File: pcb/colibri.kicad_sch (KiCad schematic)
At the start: 93 parts

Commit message: starting to build the right side
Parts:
- added pro-micro2: ProMicro, kbd:ProMicro_v4, symbol kbd:ProMicro
- added rd-1, rd-10, rd-11, rd-12, rd-13, rd-14, rd-15, rd-16, rd-17, rd-18, rd-19, rd-2, rd-20, rd-21, rd-22, rd-23, rd-24, rd-25, rd-26, rd-27, rd-3, rd-4, rd-5, rd-6, rd-7, rd-8, rd-9: 1N4148W, kbd:D3_SMD_v2, symbol Diode:1N4148W
- added rjack-1: MJ-4PP-9, kbd:MJ-4PP-9_1side, symbol kbd:MJ-4PP-9
- added rled-1, rled-10, rled-11, rled-12, rled-13, rled-14, rled-15, rled-16, rled-17, rled-18, rled-19, rled-2, rled-20, rled-21, rled-22, rled-23, rled-24, rled-25, rled-26, rled-27, rled-3, rled-4, rled-5, rled-6, rled-7, rled-8, rled-9: YS-SK6812MINI-E, kbd:YS-SK6812MINI-E, symbol kbd:YS-SK6812MINI-E
- added rreset-1: SW_PUSH, kbd:ResetSW_4P, symbol kbd:SW_PUSH
- added rsw-1: SW_PUSH, kbd:CherryMX_Hotswap_2u, symbol kbd:SW_PUSH
- added rsw-10, rsw-11, rsw-12, rsw-14, rsw-15, rsw-16, rsw-17, rsw-18, rsw-2, rsw-20, rsw-21, rsw-22, rsw-23, rsw-24, rsw-3, rsw-4, rsw-5, rsw-6, rsw-8, rsw-9: SW_PUSH, kbd:CherryMX_Hotswap, symbol kbd:SW_PUSH
- added rsw-13: SW_PUSH, kbd:CherryMX_Hotswap_2.25u, symbol kbd:SW_PUSH
- added rsw-19: SW_PUSH, kbd:CherryMX_Hotswap_2.75u, symbol kbd:SW_PUSH
- added rsw-25, rsw-26, rsw-27: SW_PUSH, kbd:CherryMX_Hotswap_1.25u, symbol kbd:SW_PUSH
- added rsw-7: SW_PUSH, kbd:CherryMX_Hotswap_1.5u, symbol kbd:SW_PUSH
- added ru-1, ru-2, ru-3, ru-4, ru-5, ru-6: WS2812B, LED_SMD:LED_WS2812B_PLCC4_5.0x5.0mm_P3.2mm, symbol LED:WS2812B
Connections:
- new net: rd-6.2 (A), rsw-6.2
- new net: rled-24.2 (DOUT), rled-27.4 (DIN)
- new net: rled-20.2 (DOUT), rled-21.4 (DIN)
- new net: rled-14.2 (DOUT), rled-20.4 (DIN)
- new net: rd-18.2 (A), rsw-18.2
- new net: rd-9.2 (A), rsw-9.2
- new net: rled-1.2 (DOUT), rled-2.4 (DIN)
- new net: rled-1.4 (DIN), rled-7.2 (DOUT)
- new net: rd-1.2 (A), rsw-1.2
- new net: rd-7.2 (A), rsw-7.2
- new net: rled-2.2 (DOUT), rled-8.4 (DIN)
- new net: rd-19.2 (A), rsw-19.2
- new net: rd-25.2 (A), rsw-25.2
- new net: rd-17.2 (A), rsw-17.2
- new net: rd-15.2 (A), rsw-15.2
- new net: rled-19.4 (DIN), ru-4.2 (DOUT)
- new net: ru-4.4 (DIN), ru-5.2 (DOUT)
- new net: rled-18.2 (DOUT), rled-24.4 (DIN)
- new net: rd-20.2 (A), rsw-20.2
- new net: rled-5.2 (DOUT), rled-6.4 (DIN)
- new net: rled-11.2 (DOUT), rled-5.4 (DIN)
- new net: rd-3.2 (A), rsw-3.2
- new net: rd-8.2 (A), rsw-8.2
- new net: ru-1.2 (DOUT), ru-2.4 (DIN)
- new net: rled-3.4 (DIN), rled-9.2 (DOUT)
- new net: rled-15.2 (DOUT), rled-9.4 (DIN)
- new net: rd-11.2 (A), rsw-11.2
- new net: rd-27.2 (A), rsw-27.2
- new net: rd-12.2 (A), rsw-12.2
- new net: rled-11.4 (DIN), rled-17.2 (DOUT)
- new net: rd-22.2 (A), rsw-22.2
- new net: rd-26.2 (A), rsw-26.2
- new net: ru-5.4 (DIN), ru-6.2 (DOUT)
- new net: rled-13.2 (DOUT), rled-7.4 (DIN)
- new net: rled-13.4 (DIN), rled-19.2 (DOUT)
- new net: rd-16.2 (A), rsw-16.2
- new net: rd-4.2 (A), rsw-4.2
- new net: rled-25.2 (DOUT), rled-26.4 (DIN)
- new net: rled-22.2 (DOUT), rled-25.4 (DIN)
- new net: ru-3.2 (DOUT), ru-6.4 (DIN)
- new net: ru-2.2 (DOUT), ru-3.4 (DIN)
- new net: rled-16.2 (DOUT), rled-22.4 (DIN)
- new net: rled-10.2 (DOUT), rled-16.4 (DIN)
- new net: rd-2.2 (A), rsw-2.2
- new net: rd-21.2 (A), rsw-21.2
- new net: rled-17.4 (DIN), rled-23.2 (DOUT)
- new net: rled-23.4 (DIN), rled-26.2 (DOUT)
- new net: rd-13.2 (A), rsw-13.2
- new net: rled-10.4 (DIN), rled-4.2 (DOUT)
- new net: rled-3.2 (DOUT), rled-4.4 (DIN)
- new net: rled-14.4 (DIN), rled-8.2 (DOUT)
- new net: rled-12.2 (DOUT), rled-18.4 (DIN)
- new net: rd-24.2 (A), rsw-24.2
- new net: rled-15.4 (DIN), rled-21.2 (DOUT)
- new net: rd-23.2 (A), rsw-23.2
- new net: rled-12.4 (DIN), rled-6.2 (DOUT)
- new net: rd-14.2 (A), rsw-14.2
- new net: rd-5.2 (A), rsw-5.2
- new net: rd-10.2 (A), rsw-10.2
- new net rGND: pro-micro2.23 (GND), pro-micro2.3 (GND), pro-micro2.4 (GND), rjack-1.C, rled-1.3 (VSS), rled-10.3 (VSS), rled-11.3 (VSS), rled-12.3 (VSS), rled-13.3 (VSS), rled-14.3 (VSS), rled-15.3 (VSS), rled-16.3 (VSS), rled-17.3 (VSS), rled-18.3 (VSS), rled-19.3 (VSS), rled-2.3 (VSS), rled-20.3 (VSS), rled-21.3 (VSS), rled-22.3 (VSS), rled-23.3 (VSS), rled-24.3 (VSS), rled-25.3 (VSS), rled-26.3 (VSS), rled-27.3 (VSS), rled-3.3 (VSS), rled-4.3 (VSS), rled-5.3 (VSS), rled-6.3 (VSS), rled-7.3 (VSS), rled-8.3 (VSS), rled-9.3 (VSS), rreset-1.2, ru-1.3 (VSS), ru-2.3 (VSS), ru-3.3 (VSS), ru-4.3 (VSS), ru-5.3 (VSS), ru-6.3 (VSS)
- new net rVCC: pro-micro2.21 (VCC), rjack-1.D, rled-1.1 (VDD), rled-10.1 (VDD), rled-11.1 (VDD), rled-12.1 (VDD), rled-13.1 (VDD), rled-14.1 (VDD), rled-15.1 (VDD), rled-16.1 (VDD), rled-17.1 (VDD), rled-18.1 (VDD), rled-19.1 (VDD), rled-2.1 (VDD), rled-20.1 (VDD), rled-21.1 (VDD), rled-22.1 (VDD), rled-23.1 (VDD), rled-24.1 (VDD), rled-25.1 (VDD), rled-26.1 (VDD), rled-27.1 (VDD), rled-3.1 (VDD), rled-4.1 (VDD), rled-5.1 (VDD), rled-6.1 (VDD), rled-7.1 (VDD), rled-8.1 (VDD), rled-9.1 (VDD), ru-1.1 (VDD), ru-2.1 (VDD), ru-3.1 (VDD), ru-4.1 (VDD), ru-5.1 (VDD), ru-6.1 (VDD)
- new net rcol0: pro-micro2.15 (B3/14), rsw-1.1, rsw-13.1, rsw-19.1, rsw-7.1
- new net rcol1: pro-micro2.16 (B1/15), rsw-14.1, rsw-2.1, rsw-20.1, rsw-8.1
- new net rcol2: pro-micro2.17 (F7/A0), rsw-15.1, rsw-21.1, rsw-3.1, rsw-9.1
- new net rcol3: pro-micro2.18 (F6/A1), rsw-10.1, rsw-16.1, rsw-22.1, rsw-25.1, rsw-4.1
- new net rcol4: pro-micro2.13 (B6/10), rsw-11.1, rsw-17.1, rsw-23.1, rsw-26.1, rsw-5.1
- new net rcol5: pro-micro2.14 (B2/16), rsw-12.1, rsw-18.1, rsw-24.1, rsw-27.1, rsw-6.1
- new net rdata: pro-micro2.2 (RX1/D2), rjack-1.B
- new net rled: pro-micro2.1 (TX0/D3), ru-1.4 (DIN)
- new net rreset: pro-micro2.22 (RST), rreset-1.1
- new net rrow0: pro-micro2.8 (5/C6), rd-1.1 (K), rd-2.1 (K), rd-3.1 (K), rd-4.1 (K), rd-5.1 (K), rd-6.1 (K)
- new net rrow1: pro-micro2.9 (6/D7), rd-10.1 (K), rd-11.1 (K), rd-12.1 (K), rd-7.1 (K), rd-8.1 (K), rd-9.1 (K)
- new net rrow2: pro-micro2.10 (7/E6), rd-13.1 (K), rd-14.1 (K), rd-15.1 (K), rd-16.1 (K), rd-17.1 (K), rd-18.1 (K)
- new net rrow3: pro-micro2.11 (8/B4), rd-19.1 (K), rd-20.1 (K), rd-21.1 (K), rd-22.1 (K), rd-23.1 (K), rd-24.1 (K)
- new net rrow4: pro-micro2.12 (9/B5), rd-25.1 (K), rd-26.1 (K), rd-27.1 (K)
- no-connect marks 8 -> 16
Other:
- note added: "Left Side"
- company: (none) -> @tangzero
- moved on the sheet: ld-1, ld-10, ld-11, ld-12, ld-13, ld-14, ld-15, ld-16, ld-17, ld-18, ld-19, ld-2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

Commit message: fix gnd and vcc symbols for left side
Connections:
- net lGND renamed GND1
- net lVCC renamed VCC

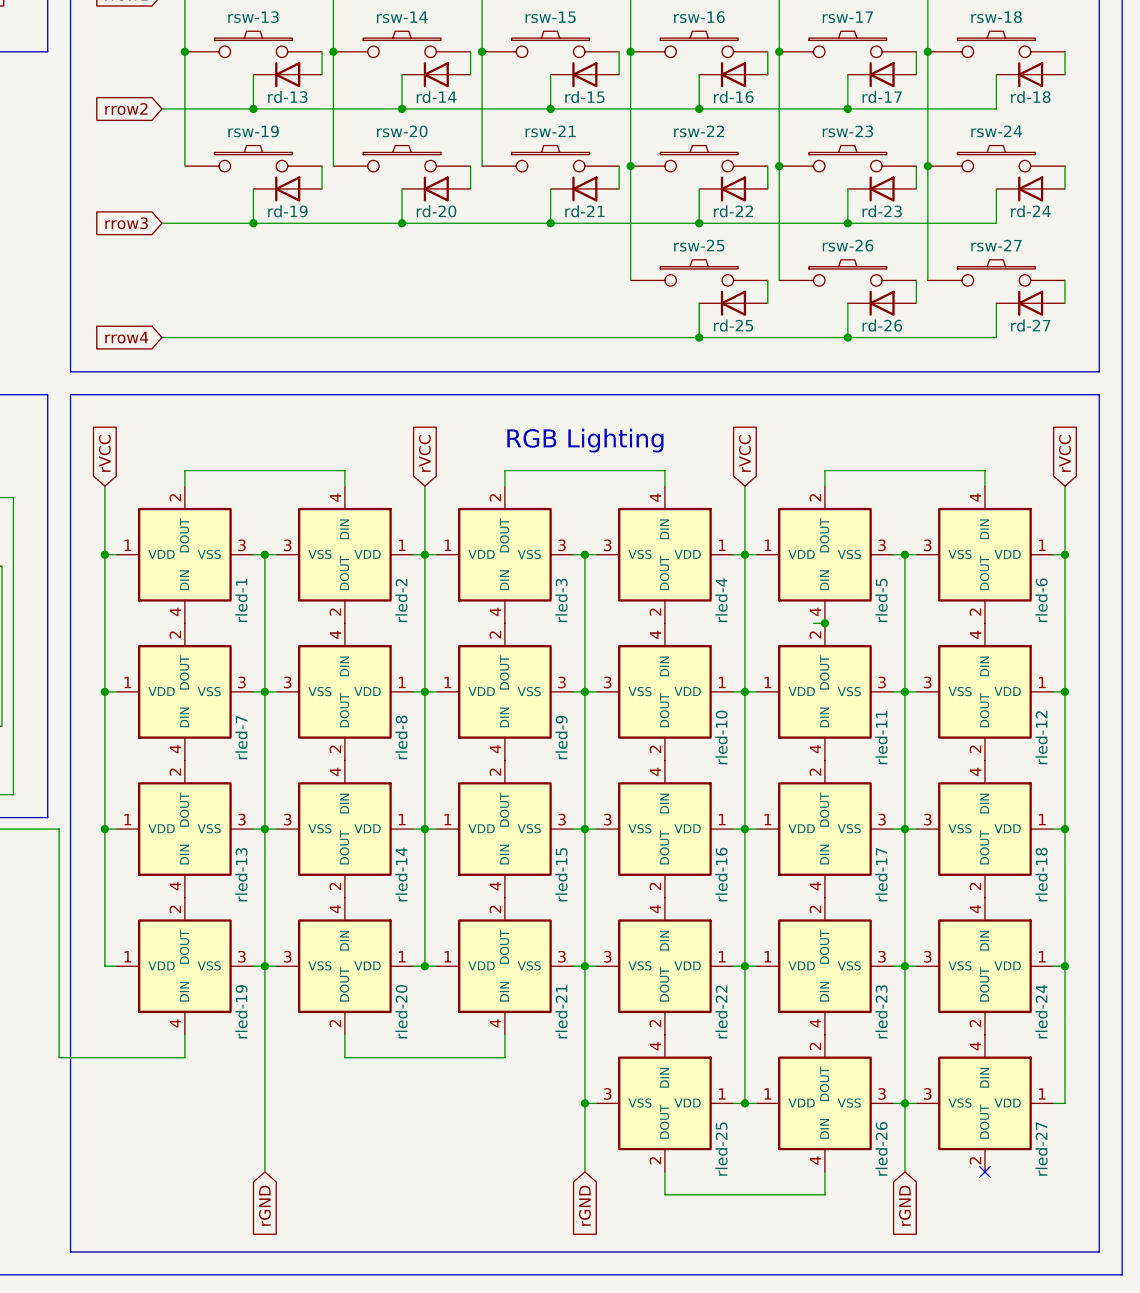
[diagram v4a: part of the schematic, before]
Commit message: added one more key to the right side
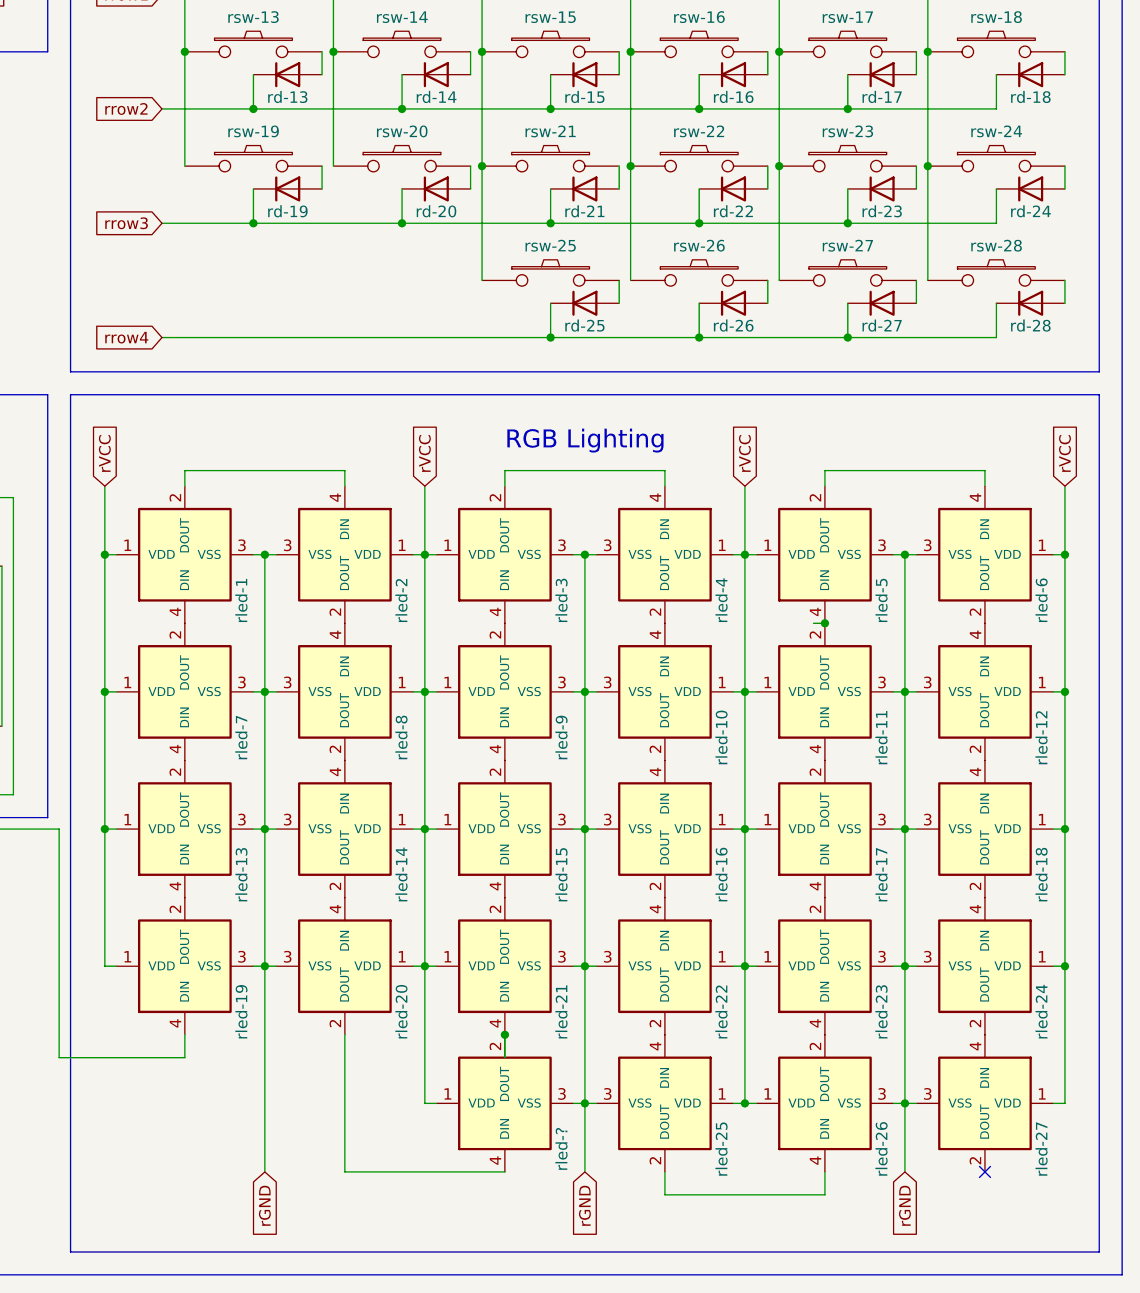
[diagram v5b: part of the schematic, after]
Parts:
- added rd-25: 1N4148W, kbd:D3_SMD_v2, symbol Diode:1N4148W
- added rled-?: YS-SK6812MINI-E, kbd:YS-SK6812MINI-E, symbol kbd:YS-SK6812MINI-E
- added rsw-25: SW_PUSH, kbd:CherryMX_Hotswap_1.25u, symbol kbd:SW_PUSH
- renumbered rd-25 to rd-26, rd-26 to rd-27, rd-27 to rd-28, rsw-25 to rsw-26, rsw-26 to rsw-27, rsw-27 to rsw-28
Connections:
- net rGND: now also rled-?.3 (VSS)
- net rVCC: now also rled-?.1 (VDD)
- net rcol2: now also rsw-25.1
- net rrow4: now also rd-25.1 (K)
- net at rled-20.2 (DOUT): now also rled-?.4 (DIN); no longer rled-21.4 (DIN)
- new net: rd-25.2 (A), rsw-25.2
- new net: rled-21.4 (DIN), rled-?.2 (DOUT)

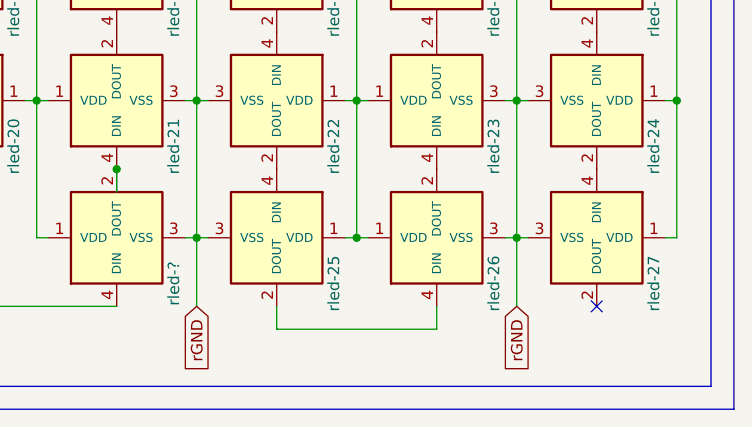
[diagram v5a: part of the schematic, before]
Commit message: fixed gnd and vcc width for left side pcb
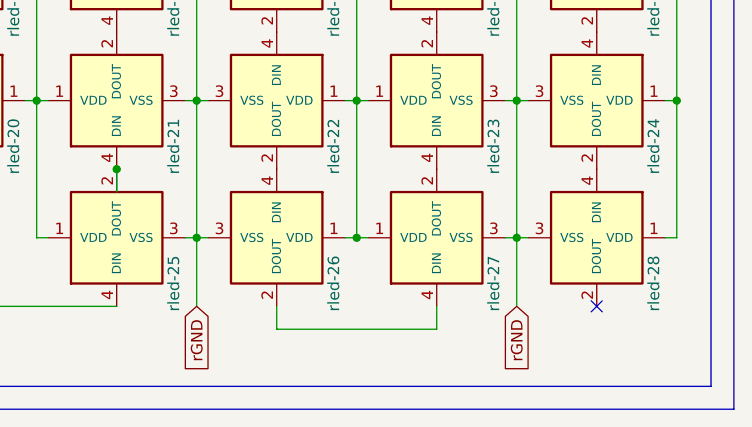
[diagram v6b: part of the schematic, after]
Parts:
- gave numbers to parts that had none: 1
- renumbered rled-25 to rled-26, rled-26 to rled-27, rled-27 to rled-28
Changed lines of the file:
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@@
   (symbol (lib_id "kbd:YS-SK6812MINI-E") (at 374.015 214.63 270) (unit 1)
     (in_bom yes) (on_board yes)
-    (property "Reference" "rled-27" (id 0) (at 380.365 219.71 0))
+    (property "Reference" "rled-28" (id 0) (at 380.365 219.71 0))
     (property "Value" "YS-SK6812MINI-E" (id 1) (at 381.635 208.28 0)
       (effects (font (size 0.7366 0.7366)) hide)
@@
   (symbol (lib_id "kbd:YS-SK6812MINI-E") (at 338.455 214.63 270) (unit 1)
     (in_bom yes) (on_board yes)
-    (property "Reference" "rled-25" (id 0) (at 344.805 219.71 0))
+    (property "Reference" "rled-26" (id 0) (at 344.805 219.71 0))
     (property "Value" "YS-SK6812MINI-E" (id 1) (at 346.075 208.28 0)
       (effects (font (size 0.7366 0.7366)) hide)
@@
   (symbol (lib_id "kbd:YS-SK6812MINI-E") (at 356.235 214.63 90) (unit 1)
     (in_bom yes) (on_board yes)
-    (property "Reference" "rled-26" (id 0) (at 362.585 219.71 0))
+    (property "Reference" "rled-27" (id 0) (at 362.585 219.71 0))
     (property "Value" "YS-SK6812MINI-E" (id 1) (at 363.855 208.28 0)
       (effects (font (size 0.7366 0.7366)) hide)
@@
   (symbol (lib_id "kbd:YS-SK6812MINI-E") (at 320.675 214.63 90) (unit 1)
     (in_bom yes) (on_board yes)
-    (property "Reference" "rled-?" (id 0) (at 327.025 219.71 0))
+    (property "Reference" "rled-25" (id 0) (at 327.025 219.71 0))
     (property "Value" "YS-SK6812MINI-E" (id 1) (at 328.295 208.28 0)
       (effects (font (size 0.7366 0.7366)) hide)
@@
       (reference "rled-24") (unit 1) (value "YS-SK6812MINI-E") (footprint "kbd:YS-SK6812MINI-E")
     )
-    (path "/5bf13ea5-6457-421f-ba3e-dad4ac2a8516"
+    (path "/b48e295e-83d4-4eed-879c-1146f3a47f15"
       (reference "rled-25") (unit 1) (value "YS-SK6812MINI-E") (footprint "kbd:YS-SK6812MINI-E")
     )
-    (path "/8afd761c-2efa-4d02-881f-a197f486f3bd"
+    (path "/5bf13ea5-6457-421f-ba3e-dad4ac2a8516"
       (reference "rled-26") (unit 1) (value "YS-SK6812MINI-E") (footprint "kbd:YS-SK6812MINI-E")
     )
-    (path "/0816d4d0-16a3-4d36-9322-f7a6c6db27ad"
+    (path "/8afd761c-2efa-4d02-881f-a197f486f3bd"
       (reference "rled-27") (unit 1) (value "YS-SK6812MINI-E") (footprint "kbd:YS-SK6812MINI-E")
     )
-    (path "/b48e295e-83d4-4eed-879c-1146f3a47f15"
-      (reference "rled-?") (unit 1) (value "YS-SK6812MINI-E") (footprint "kbd:YS-SK6812MINI-E")
+    (path "/0816d4d0-16a3-4d36-9322-f7a6c6db27ad"
+      (reference "rled-28") (unit 1) (value "YS-SK6812MINI-E") (footprint "kbd:YS-SK6812MINI-E")
     )
     (path "/9f6f9623-ce68-4e21-ac2f-884b8146f2ae"

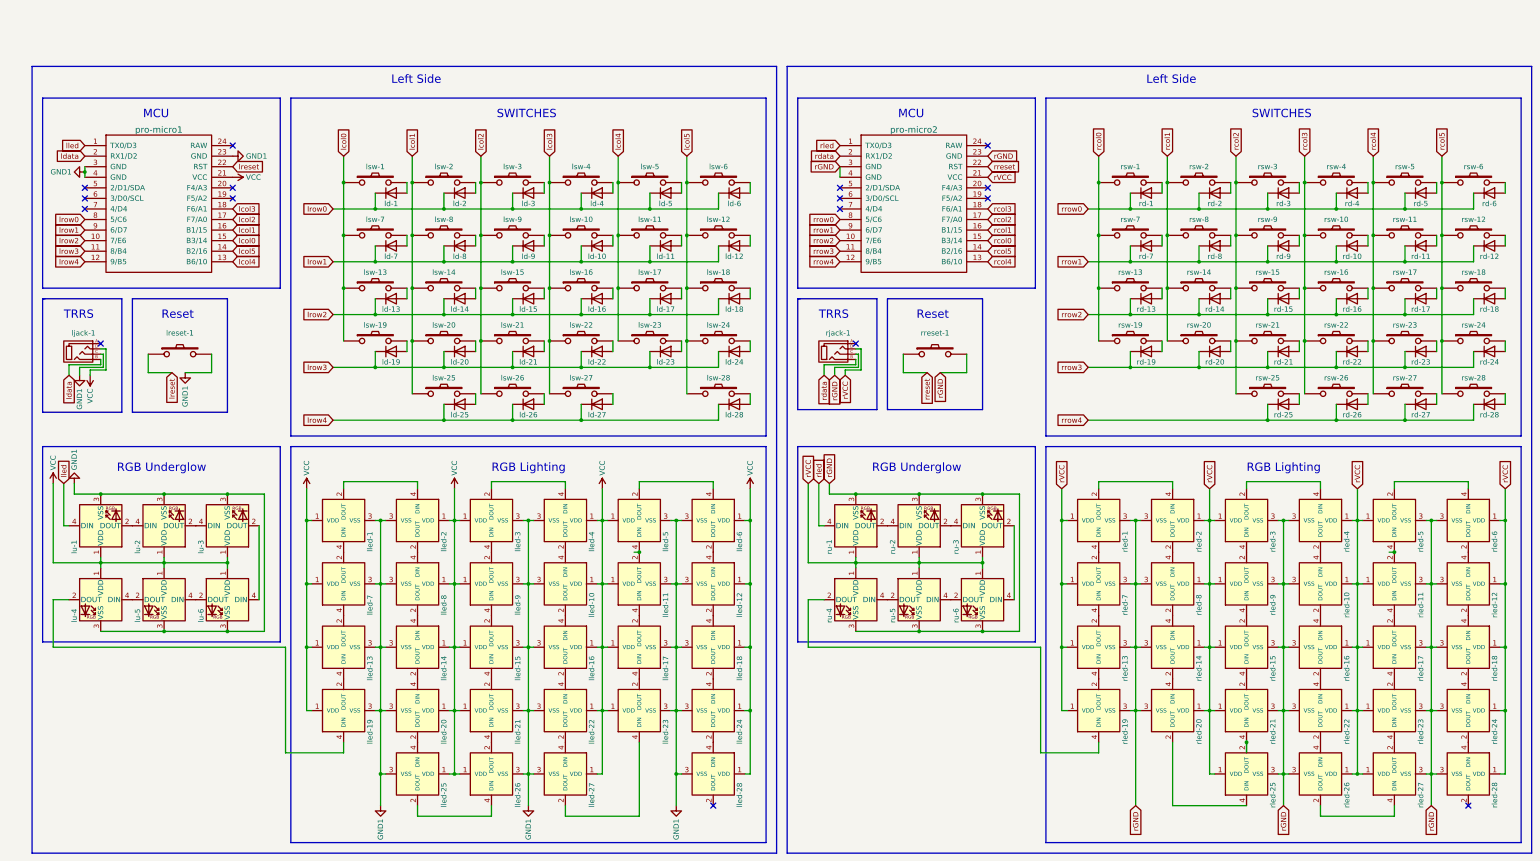
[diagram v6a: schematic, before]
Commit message: rows connected on the right side
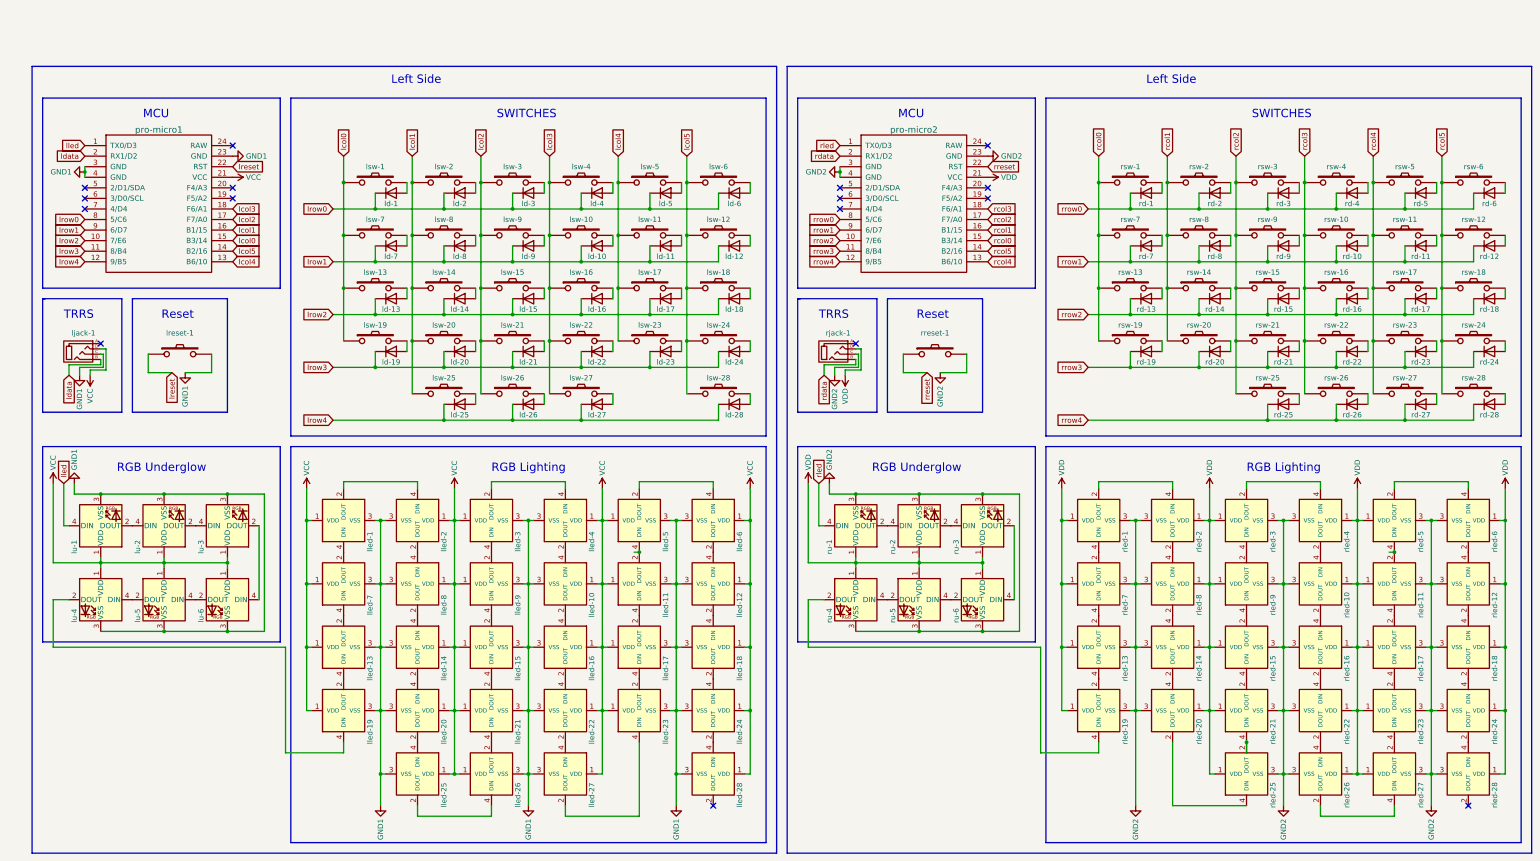
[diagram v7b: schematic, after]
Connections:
- net rGND renamed GND2
- net rVCC renamed VDD
